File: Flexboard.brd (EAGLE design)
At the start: 488.2 x 145.3 mm, 452 parts, among them J1 USB4105-GF-A, SW1 1825910-7, U1 MK22FX512AVLQ12, U2 NCP1117ST33T3G, Y1 ABM3B-8.000MHZ-B2-T, Y2 ABS07-32.768KHZ-T

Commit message: added four media keys
added four additional media keys to board, and renumbered keys to
perserve correct numbering sequence.

Signed-off-by: Daniel DeGrasse <daniel@degrasse.com>
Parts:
- added D147, D148, D149: BAS16LT3G, BAS16LT3G:SOT95P240X111-3N
- added D150: UPS115UE3/TR7, UPS115UE3-TR7:UPS115UE3/TR7
- added KEY_146, KEY_147, KEY_148, KEY_149: CHERRY-MX-LED, cherrymx:CHERRY-MX-LED
- D146: value UPS115UE3/TR7 -> BAS16LT3G; device UPS115UE3-TR7:UPS115UE3/TR7 -> BAS16LT3G:SOT95P240X111-3N
- moved D41 411.1 mm to (428.6, 119.1)
- moved D42 411.1 mm to (447.7, 119.1)
- moved KEY_41 410.6 mm to (419.1, 114.3)
- moved KEY_42 410.6 mm to (438.1, 114.3)
- moved KEY_109 410.0 mm to (419.1, 47.6)
- moved KEY_64 410.0 mm to (419.1, 85.7)
- moved KEY_87 410.0 mm to (419.1, 66.7)
- moved D109 410.0 mm to (428.6, 45.2)
- moved D110 410.0 mm to (447.7, 45.2)
- moved D64 410.0 mm to (428.6, 83.3)
- moved D65 410.0 mm to (447.7, 83.3)
- moved D87 410.0 mm to (428.6, 64.3)
- moved D88 410.0 mm to (447.7, 64.3)
- moved KEY_110 410.0 mm to (438.1, 47.6)
- moved KEY_65 410.0 mm to (438.1, 85.7)
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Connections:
- new net N$155: D149.3, KEY_149.SW2
- new net N$159: D146.3, KEY_146.SW2
- new net N$161: D148.3, KEY_148.SW2
- new net N$165: D147.3, KEY_147.SW2
- net COL_10: now also KEY_100.SW1, KEY_122.SW1, KEY_54.SW1, KEY_77.SW1; no longer KEY_118.SW1, KEY_50.SW1, KEY_73.SW1, KEY_96.SW1
- net COL_11: now also KEY_101.SW1, KEY_123.SW1, KEY_55.SW1, KEY_78.SW1; no longer KEY_119.SW1, KEY_51.SW1, KEY_74.SW1, KEY_97.SW1
- net COL_12: now also KEY_102.SW1, KEY_124.SW1, KEY_139.SW1, KEY_56.SW1, KEY_79.SW1; no longer KEY_120.SW1, KEY_135.SW1, KEY_52.SW1, KEY_75.SW1, KEY_98.SW1
- net COL_13: now also KEY_103.SW1, KEY_125.SW1, KEY_140.SW1, KEY_57.SW1, KEY_80.SW1; no longer KEY_121.SW1, KEY_136.SW1, KEY_53.SW1, KEY_76.SW1, KEY_99.SW1
- net COL_14: now also KEY_104.SW1, KEY_141.SW1, KEY_58.SW1, KEY_81.SW1; no longer KEY_100.SW1, KEY_137.SW1, KEY_54.SW1, KEY_77.SW1
- net COL_15: now also KEY_59.SW1, KEY_82.SW1; no longer KEY_55.SW1, KEY_78.SW1
- net COL_17: now also KEY_105.SW1, KEY_126.SW1, KEY_142.SW1, KEY_60.SW1, KEY_83.SW1; no longer KEY_101.SW1, KEY_122.SW1, KEY_138.SW1, KEY_56.SW1, KEY_79.SW1
- net COL_18: now also KEY_106.SW1, KEY_127.SW1, KEY_143.SW1, KEY_61.SW1, KEY_84.SW1; no longer KEY_102.SW1, KEY_123.SW1, KEY_139.SW1, KEY_57.SW1, KEY_80.SW1
- net COL_19: now also KEY_107.SW1, KEY_128.SW1, KEY_144.SW1, KEY_62.SW1, KEY_85.SW1; no longer KEY_103.SW1, KEY_124.SW1, KEY_140.SW1, KEY_58.SW1, KEY_81.SW1
- net COL_1{SB}: now also KEY_113.SW1, KEY_133.SW1, KEY_45.SW1, KEY_68.SW1, KEY_91.SW1; no longer KEY_109.SW1, KEY_129.SW1, KEY_41.SW1, KEY_64.SW1, KEY_87.SW1
- net COL_20: now also KEY_108.SW1, KEY_129.SW1, KEY_145.SW1, KEY_63.SW1, KEY_86.SW1; no longer KEY_104.SW1, KEY_125.SW1, KEY_141.SW1, KEY_59.SW1, KEY_82.SW1
- net COL_21: now also KEY_109.SW1, KEY_130.SW1, KEY_146.SW1, KEY_41.SW1, KEY_64.SW1, KEY_87.SW1; no longer KEY_105.SW1, KEY_126.SW1, KEY_142.SW1, KEY_60.SW1, KEY_83.SW1
- net COL_22: now also KEY_110.SW1, KEY_131.SW1, KEY_147.SW1, KEY_42.SW1, KEY_65.SW1, KEY_88.SW1; no longer KEY_106.SW1, KEY_127.SW1, KEY_143.SW1, KEY_61.SW1, KEY_84.SW1
- net COL_23: now also KEY_111.SW1, KEY_132.SW1, KEY_148.SW1, KEY_43.SW1, KEY_66.SW1, KEY_89.SW1; no longer KEY_107.SW1, KEY_128.SW1, KEY_144.SW1, KEY_62.SW1, KEY_85.SW1
- net COL_24: now also KEY_112.SW1, KEY_149.SW1, KEY_44.SW1, KEY_67.SW1, KEY_90.SW1; no longer KEY_108.SW1, KEY_145.SW1, KEY_63.SW1, KEY_86.SW1
- net COL_2{SB}: now also KEY_114.SW1, KEY_134.SW1, KEY_46.SW1, KEY_69.SW1, KEY_92.SW1; no longer KEY_110.SW1, KEY_130.SW1, KEY_42.SW1, KEY_65.SW1, KEY_88.SW1
- net COL_3: now also KEY_115.SW1, KEY_135.SW1, KEY_47.SW1, KEY_70.SW1, KEY_93.SW1; no longer KEY_111.SW1, KEY_131.SW1, KEY_43.SW1, KEY_66.SW1, KEY_89.SW1
- net COL_4: now also KEY_116.SW1, KEY_136.SW1, KEY_48.SW1, KEY_71.SW1, KEY_94.SW1; no longer KEY_112.SW1, KEY_132.SW1, KEY_44.SW1, KEY_67.SW1, KEY_90.SW1
- net COL_5: now also KEY_117.SW1, KEY_137.SW1, KEY_49.SW1, KEY_72.SW1, KEY_95.SW1; no longer KEY_113.SW1, KEY_133.SW1, KEY_45.SW1, KEY_68.SW1, KEY_91.SW1
- net COL_6: now also KEY_118.SW1, KEY_50.SW1, KEY_73.SW1, KEY_96.SW1; no longer KEY_114.SW1, KEY_46.SW1, KEY_69.SW1, KEY_92.SW1
- net COL_7: now also KEY_119.SW1, KEY_51.SW1, KEY_74.SW1, KEY_97.SW1; no longer KEY_115.SW1, KEY_47.SW1, KEY_70.SW1, KEY_93.SW1
- net COL_8: now also KEY_120.SW1, KEY_138.SW1, KEY_52.SW1, KEY_75.SW1, KEY_98.SW1; no longer KEY_116.SW1, KEY_134.SW1, KEY_48.SW1, KEY_71.SW1, KEY_94.SW1
- net COL_9: now also KEY_121.SW1, KEY_53.SW1, KEY_76.SW1, KEY_99.SW1; no longer KEY_117.SW1, KEY_49.SW1, KEY_72.SW1, KEY_95.SW1
- net LED_COL_10: now also KEY_100.LED-, KEY_122.LED-, KEY_54.LED-, KEY_77.LED-; no longer KEY_118.LED-, KEY_50.LED-, KEY_73.LED-, KEY_96.LED-
- net LED_COL_11: now also KEY_101.LED-, KEY_123.LED-, KEY_55.LED-, KEY_78.LED-; no longer KEY_119.LED-, KEY_51.LED-, KEY_74.LED-, KEY_97.LED-
- net LED_COL_12: now also KEY_102.LED-, KEY_124.LED-, KEY_139.LED-, KEY_56.LED-, KEY_79.LED-; no longer KEY_120.LED-, KEY_135.LED-, KEY_52.LED-, KEY_75.LED-, KEY_98.LED-
- net LED_COL_13: now also KEY_103.LED-, KEY_125.LED-, KEY_140.LED-, KEY_57.LED-, KEY_80.LED-; no longer KEY_121.LED-, KEY_136.LED-, KEY_53.LED-, KEY_76.LED-, KEY_99.LED-
- net LED_COL_14: now also KEY_104.LED-, KEY_141.LED-, KEY_58.LED-, KEY_81.LED-; no longer KEY_100.LED-, KEY_137.LED-, KEY_54.LED-, KEY_77.LED-
- net LED_COL_15: now also KEY_59.LED-, KEY_82.LED-; no longer KEY_55.LED-, KEY_78.LED-
- net LED_COL_17: now also KEY_105.LED-, KEY_126.LED-, KEY_142.LED-, KEY_60.LED-, KEY_83.LED-; no longer KEY_101.LED-, KEY_122.LED-, KEY_138.LED-, KEY_56.LED-, KEY_79.LED-
- net LED_COL_18: now also KEY_106.LED-, KEY_127.LED-, KEY_143.LED-, KEY_61.LED-, KEY_84.LED-; no longer KEY_102.LED-, KEY_123.LED-, KEY_139.LED-, KEY_57.LED-, KEY_80.LED-
- net LED_COL_19: now also KEY_107.LED-, KEY_128.LED-, KEY_144.LED-, KEY_62.LED-, KEY_85.LED-; no longer KEY_103.LED-, KEY_124.LED-, KEY_140.LED-, KEY_58.LED-, KEY_81.LED-
- net LED_COL_1{SB}: now also KEY_113.LED-, KEY_133.LED-, KEY_45.LED-, KEY_68.LED-, KEY_91.LED-; no longer KEY_109.LED-, KEY_129.LED-, KEY_41.LED-, KEY_64.LED-, KEY_87.LED-
- net LED_COL_20: now also KEY_108.LED-, KEY_129.LED-, KEY_145.LED-, KEY_63.LED-, KEY_86.LED-; no longer KEY_104.LED-, KEY_125.LED-, KEY_141.LED-, KEY_59.LED-, KEY_82.LED-
- net LED_COL_21: now also KEY_109.LED-, KEY_130.LED-, KEY_146.LED-, KEY_41.LED-, KEY_64.LED-, KEY_87.LED-; no longer KEY_105.LED-, KEY_126.LED-, KEY_142.LED-, KEY_60.LED-, KEY_83.LED-
- net LED_COL_22: now also KEY_110.LED-, KEY_131.LED-, KEY_147.LED-, KEY_42.LED-, KEY_65.LED-, KEY_88.LED-; no longer KEY_106.LED-, KEY_127.LED-, KEY_143.LED-, KEY_61.LED-, KEY_84.LED-
- net LED_COL_23: now also KEY_111.LED-, KEY_132.LED-, KEY_148.LED-, KEY_43.LED-, KEY_66.LED-, KEY_89.LED-; no longer KEY_107.LED-, KEY_128.LED-, KEY_144.LED-, KEY_62.LED-, KEY_85.LED-
- net LED_COL_24: now also KEY_112.LED-, KEY_149.LED-, KEY_44.LED-, KEY_67.LED-, KEY_90.LED-; no longer KEY_108.LED-, KEY_145.LED-, KEY_63.LED-, KEY_86.LED-
- net LED_COL_2{SB}: now also KEY_114.LED-, KEY_134.LED-, KEY_46.LED-, KEY_69.LED-, KEY_92.LED-; no longer KEY_110.LED-, KEY_130.LED-, KEY_42.LED-, KEY_65.LED-, KEY_88.LED-
- net LED_COL_3: now also KEY_115.LED-, KEY_135.LED-, KEY_47.LED-, KEY_70.LED-, KEY_93.LED-; no longer KEY_111.LED-, KEY_131.LED-, KEY_43.LED-, KEY_66.LED-, KEY_89.LED-
- net LED_COL_4: now also KEY_116.LED-, KEY_136.LED-, KEY_48.LED-, KEY_71.LED-, KEY_94.LED-; no longer KEY_112.LED-, KEY_132.LED-, KEY_44.LED-, KEY_67.LED-, KEY_90.LED-
- net LED_COL_5: now also KEY_117.LED-, KEY_49.LED-, KEY_72.LED-, KEY_95.LED-; no longer KEY_113.LED-, KEY_45.LED-, KEY_68.LED-, KEY_91.LED-
- net LED_COL_6: now also KEY_118.LED-, KEY_50.LED-, KEY_73.LED-, KEY_96.LED-; no longer KEY_114.LED-, KEY_46.LED-, KEY_69.LED-, KEY_92.LED-
- net LED_COL_7: now also KEY_119.LED-, KEY_51.LED-, KEY_74.LED-, KEY_97.LED-; no longer KEY_115.LED-, KEY_47.LED-, KEY_70.LED-, KEY_93.LED-
- net LED_COL_8: now also KEY_120.LED-, KEY_138.LED-, KEY_52.LED-, KEY_75.LED-, KEY_98.LED-; no longer KEY_116.LED-, KEY_134.LED-, KEY_48.LED-, KEY_71.LED-, KEY_94.LED-
- net LED_COL_9: now also KEY_121.LED-, KEY_53.LED-, KEY_76.LED-, KEY_99.LED-; no longer KEY_117.LED-, KEY_49.LED-, KEY_72.LED-, KEY_95.LED-
- net LED_ROW_2{SB}: now also KEY_41.LED+, KEY_42.LED+, KEY_43.LED+, KEY_44.LED+
- net LED_ROW_3: now also KEY_45.LED+, KEY_46.LED+; no longer KEY_41.LED+, KEY_42.LED+
- net LED_ROW_3{SB}: now also KEY_60.LED+, KEY_61.LED+, KEY_62.LED+, KEY_63.LED+; no longer KEY_43.LED+, KEY_44.LED+, KEY_45.LED+, KEY_46.LED+
- net LED_ROW_4: now also KEY_68.LED+, KEY_69.LED+; no longer KEY_64.LED+, KEY_65.LED+
- net LED_ROW_4{SB}: now also KEY_83.LED+, KEY_84.LED+, KEY_85.LED+, KEY_86.LED+; no longer KEY_66.LED+, KEY_67.LED+, KEY_68.LED+, KEY_69.LED+
- net LED_ROW_5: now also KEY_91.LED+, KEY_92.LED+; no longer KEY_87.LED+, KEY_88.LED+
- net LED_ROW_5{SB}: now also KEY_105.LED+, KEY_106.LED+, KEY_107.LED+, KEY_108.LED+; no longer KEY_89.LED+, KEY_90.LED+, KEY_91.LED+, KEY_92.LED+
- net LED_ROW_6: now also KEY_113.LED+, KEY_114.LED+; no longer KEY_109.LED+, KEY_110.LED+
- net LED_ROW_6{SB}: now also KEY_126.LED+, KEY_127.LED+, KEY_128.LED+, KEY_129.LED+; no longer KEY_111.LED+, KEY_112.LED+, KEY_113.LED+, KEY_114.LED+
- net LED_ROW_7: now also KEY_133.LED+, KEY_134.LED+; no longer KEY_129.LED+, KEY_130.LED+
- net LED_ROW_7{SB}: now also KEY_142.LED+, KEY_143.LED+, KEY_144.LED+, KEY_145.LED+; no longer KEY_131.LED+, KEY_132.LED+, KEY_133.LED+, KEY_134.LED+
- net N$103: now also D109.1, D110.1, D111.1, D112.1; no longer D105.1, D106.1, D107.1, D108.1
- net N$124: now also D130.1, D131.1, D132.1; no longer D126.1, D127.1, D128.1
- net N$151: now also D146.1, D147.1, D148.1, D149.1; no longer D142.1, D143.1, D144.1, D145.1
- net N$170: now also KEY_64.LED+, KEY_65.LED+, KEY_66.LED+, KEY_67.LED+; no longer KEY_60.LED+, KEY_61.LED+, KEY_62.LED+, KEY_63.LED+
- net N$173: now also KEY_87.LED+, KEY_88.LED+, KEY_89.LED+, KEY_90.LED+; no longer KEY_83.LED+, KEY_84.LED+, KEY_85.LED+, KEY_86.LED+
- net N$179: now also KEY_109.LED+, KEY_110.LED+, KEY_111.LED+, KEY_112.LED+; no longer KEY_105.LED+, KEY_106.LED+, KEY_107.LED+, KEY_108.LED+
- net N$182: now also KEY_130.LED+, KEY_131.LED+, KEY_132.LED+; no longer KEY_126.LED+, KEY_127.LED+, KEY_128.LED+
- net N$185: now also KEY_146.LED+, KEY_147.LED+, KEY_148.LED+, KEY_149.LED+; no longer KEY_142.LED+, KEY_143.LED+, KEY_144.LED+, KEY_145.LED+
- net N$65: now also D64.1, D65.1, D66.1, D67.1; no longer D60.1, D61.1, D62.1, D63.1
- net N$79: now also D87.1, D88.1, D89.1, D90.1; no longer D83.1, D84.1, D85.1, D86.1
- net ROW_2{SB}: now also D41.1, D42.1, D43.1, D44.1
- net ROW_3: now also D45.1, D46.1; no longer D41.1, D42.1
- net ROW_3{SB}: now also D60.1, D61.1, D62.1, D63.1; no longer D43.1, D44.1, D45.1, D46.1
- net ROW_4: now also D68.1, D69.1; no longer D64.1, D65.1
- net ROW_4{SB}: now also D83.1, D84.1, D85.1, D86.1; no longer D66.1, D67.1, D68.1, D69.1
- net ROW_5: now also D91.1, D92.1; no longer D87.1, D88.1
- net ROW_5{SB}: now also D105.1, D106.1, D107.1, D108.1; no longer D89.1, D90.1, D91.1, D92.1
- net ROW_6: now also D113.1, D114.1; no longer D109.1, D110.1
- net ROW_6{SB}: now also D126.1, D127.1, D128.1, D129.1; no longer D111.1, D112.1, D113.1, D114.1
- net ROW_7: now also D133.1, D134.1; no longer D129.1, D130.1
- net ROW_7{SB}: now also D142.1, D143.1, D144.1, D145.1; no longer D131.1, D132.1, D133.1, D134.1
- net VLDO_5V5: now also D150.1; no longer D146.1
- net VSYS_5V5: now also D150.2; no longer D146.2
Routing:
- net ROW_2{SB}: track 375.2 -> 469.2 mm
- net LED_ROW_2{SB}: track 377.3 -> 466.8 mm
- net COL_24: track 99.6 -> 129.2 mm
- net COL_22: track 91.9 -> 121.3 mm
- net COL_21: track 88.7 -> 117.7 mm
- net COL_23: track 90.7 -> 115.4 mm, vias 0 -> 1
- net LED_COL_23: track 110.0 -> 131.3 mm
- net LED_COL_24: track 117.9 -> 139.0 mm
- net LED_COL_22: track 107.2 -> 127.5 mm
- net LED_COL_21: track 106.9 -> 127.1 mm
- net N$165: track 0.00 -> 11.2 mm
- net N$161: track 0.00 -> 11.2 mm
- net N$159: track 0.00 -> 11.2 mm
- net N$89: track 11.2 -> 0.00 mm
- net N$147: track 4.31 -> 11.2 mm
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
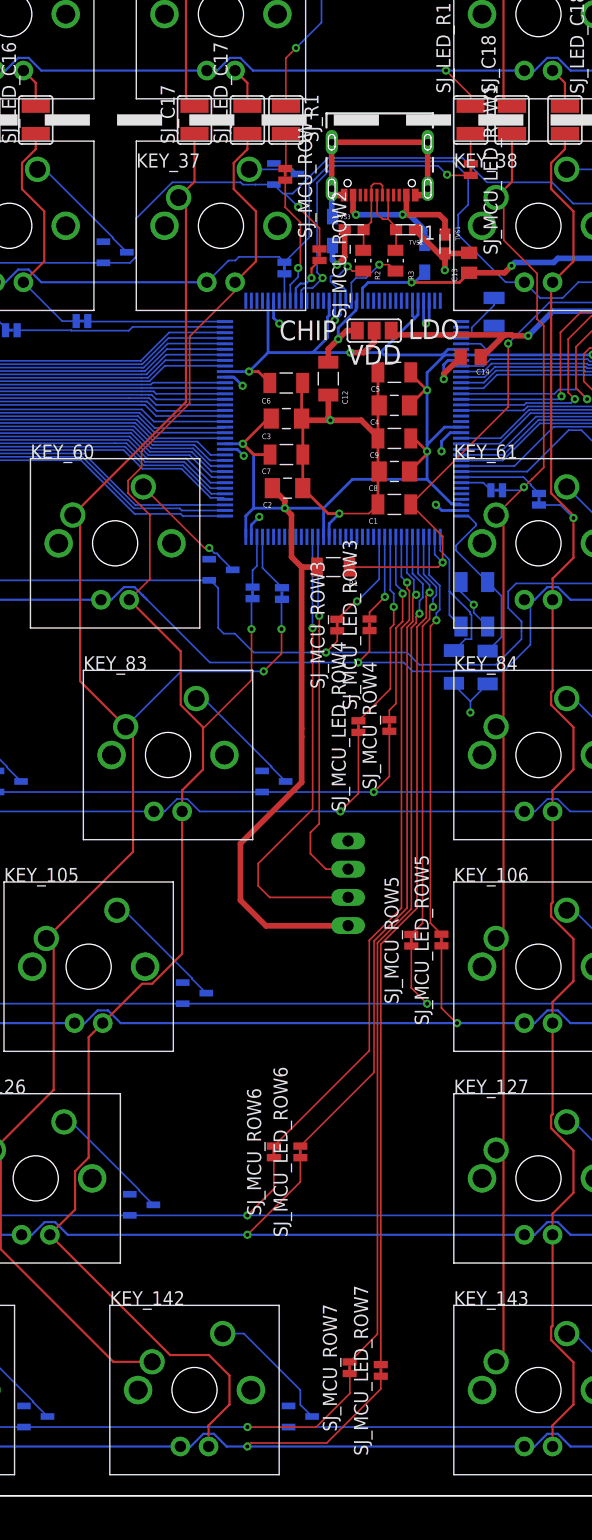
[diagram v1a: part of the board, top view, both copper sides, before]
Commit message: added current limiting resistors to LED rows
current limit resistors should limit LED network to 10mA across each
LED, for a total of roughly 70mA sourced from the chip.

Signed-off-by: Daniel DeGrasse <daniel@degrasse.com>
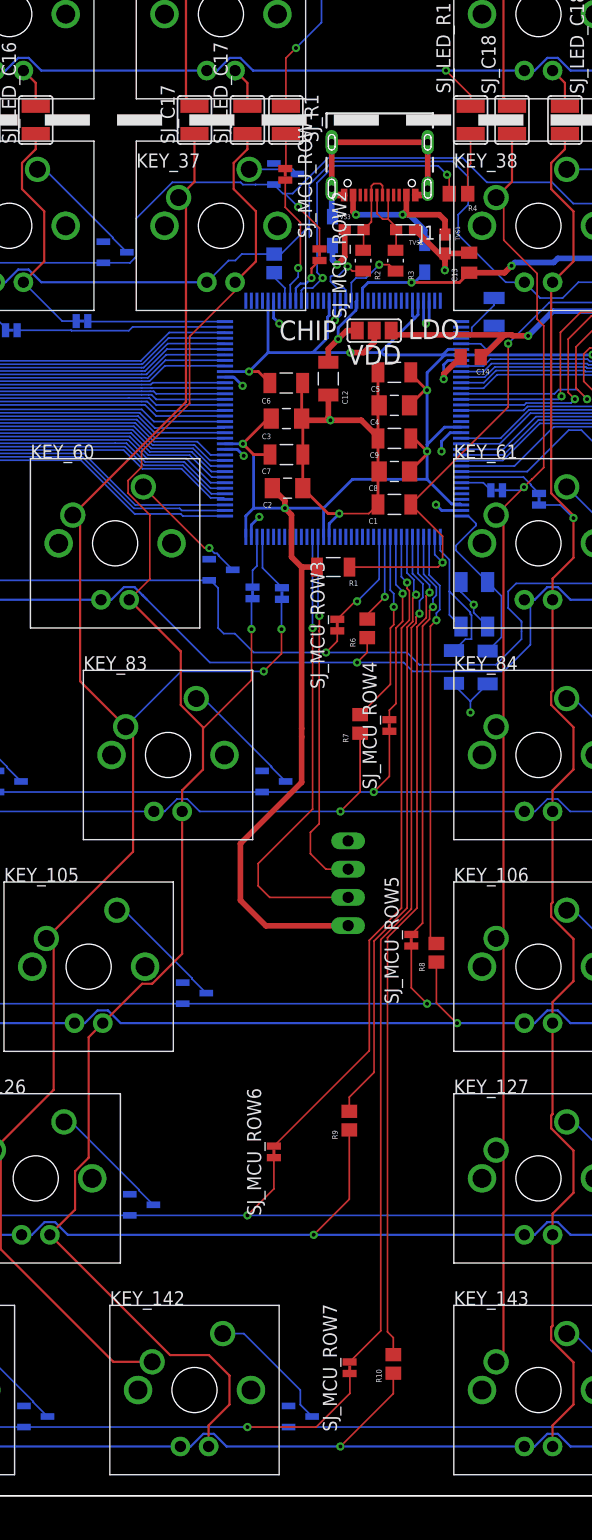
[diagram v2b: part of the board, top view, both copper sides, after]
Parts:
- removed SJ_MCU_LED_ROW1, SJ_MCU_LED_ROW2, SJ_MCU_LED_ROW3, SJ_MCU_LED_ROW4, SJ_MCU_LED_ROW5, SJ_MCU_LED_ROW6, SJ_MCU_LED_ROW7: JUMPER-SMT_2_NC_TRACE_NO-SILK, SparkFun-Jumpers:SMT-JUMPER_2_NC_TRACE_NO-SILK
- added R10, R4, R5, R6, R7, R8, R9: RNCP0805FTD20R0, RNCP0805FTD20R0:RESC2012X60N
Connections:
- net LED_ROW_1{MCU}: now also R4.2; no longer SJ_MCU_LED_ROW1.2
- net LED_ROW_1{SB}: now also R4.1; no longer SJ_MCU_LED_ROW1.1
- net LED_ROW_2{MCU}: now also R5.2; no longer SJ_MCU_LED_ROW2.2
- net LED_ROW_2{SB}: now also R5.1; no longer SJ_MCU_LED_ROW2.1
- net LED_ROW_3{MCU}: now also R6.2; no longer SJ_MCU_LED_ROW3.2
- net LED_ROW_3{SB}: now also R6.1; no longer SJ_MCU_LED_ROW3.1
- net LED_ROW_4{MCU}: now also R7.2; no longer SJ_MCU_LED_ROW4.2
- net LED_ROW_4{SB}: now also R7.1; no longer SJ_MCU_LED_ROW4.1
- net LED_ROW_5{MCU}: now also R8.2; no longer SJ_MCU_LED_ROW5.2
- net LED_ROW_5{SB}: now also R8.1; no longer SJ_MCU_LED_ROW5.1
- net LED_ROW_6{MCU}: now also R9.2; no longer SJ_MCU_LED_ROW6.2
- net LED_ROW_6{SB}: now also R9.1; no longer SJ_MCU_LED_ROW6.1
- net LED_ROW_7{MCU}: now also R10.2; no longer SJ_MCU_LED_ROW7.2
- net LED_ROW_7{SB}: now also R10.1; no longer SJ_MCU_LED_ROW7.1
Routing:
- net LED_ROW_7{SB}: track 380.5 -> 373.8 mm
- net LED_ROW_6{MCU}: track 59.5 -> 54.5 mm
- net LED_ROW_1{SB}: track 2.68 -> 5.47 mm
- net LED_ROW_6{SB}: track 379.6 -> 381.5 mm
- net LED_ROW_5{SB}: track 380.3 -> 379.0 mm
- net LED_ROW_7{MCU}: track 76.7 -> 75.8 mm
- net LED_ROW_5{MCU}: track 36.9 -> 37.6 mm
- net LED_ROW_4{MCU}: track 18.0 -> 17.4 mm
- net LED_ROW_3{SB}: track 385.3 -> 384.8 mm

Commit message: cleaned up name locations on board
cleaned up name locations on board silkscreen to ensure that there will
not be overlap between board printing and solder pads

Signed-off-by: Daniel DeGrasse <daniel@degrasse.com>
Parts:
- renumbered U$1 to J2
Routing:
- net N$89: track 0.00 -> 4.44 mm
- net ROW_4{SB}: track 381.1 -> 376.7 mm
- net LED_ROW_2{SB}: track 466.8 -> 465.8 mm
- net COL_2{SB}: track 150.3 -> 149.7 mm
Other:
- board text added: "U1"
- board text removed: "Cut Point"

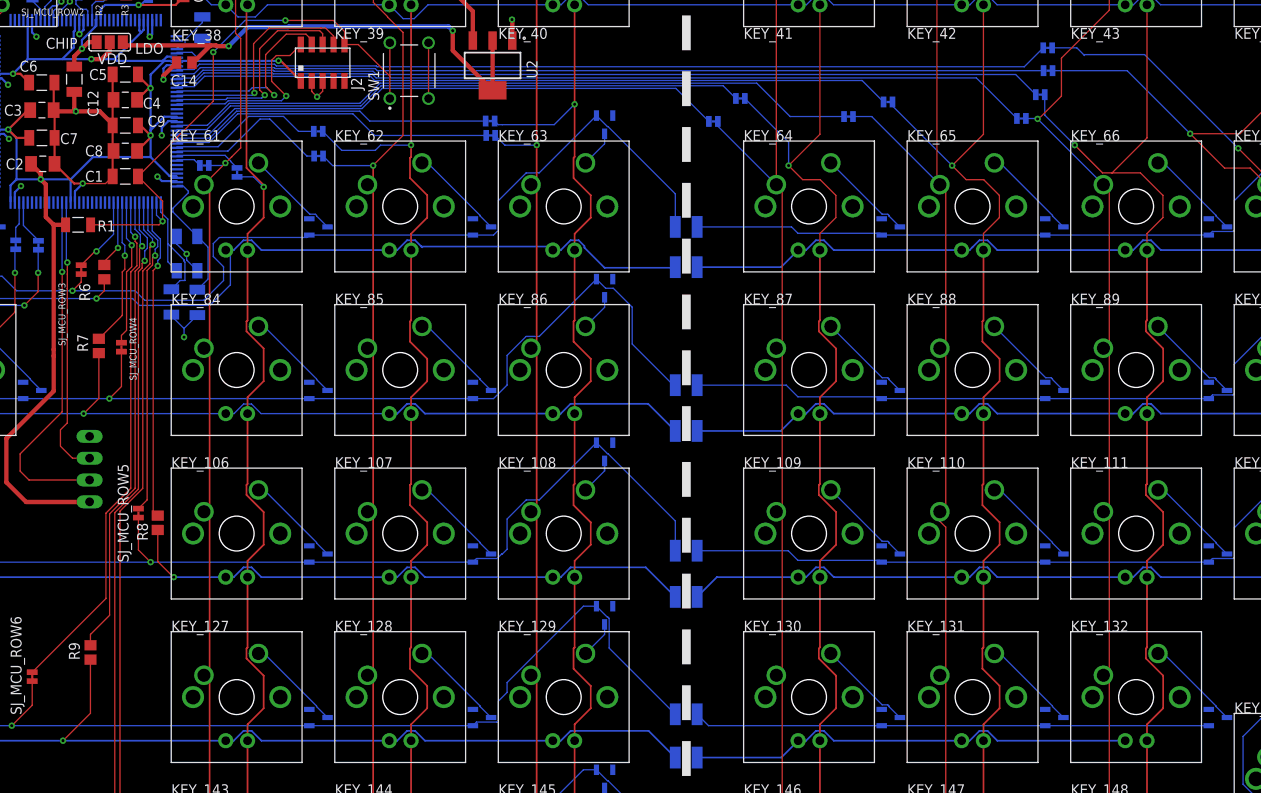
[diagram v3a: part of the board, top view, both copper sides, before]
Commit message: Fixed ERC errors
Fixed valid ERC errors, and approved remaining overlap warnings as
nonissues

Signed-off-by: Daniel DeGrasse <daniel@degrasse.com>
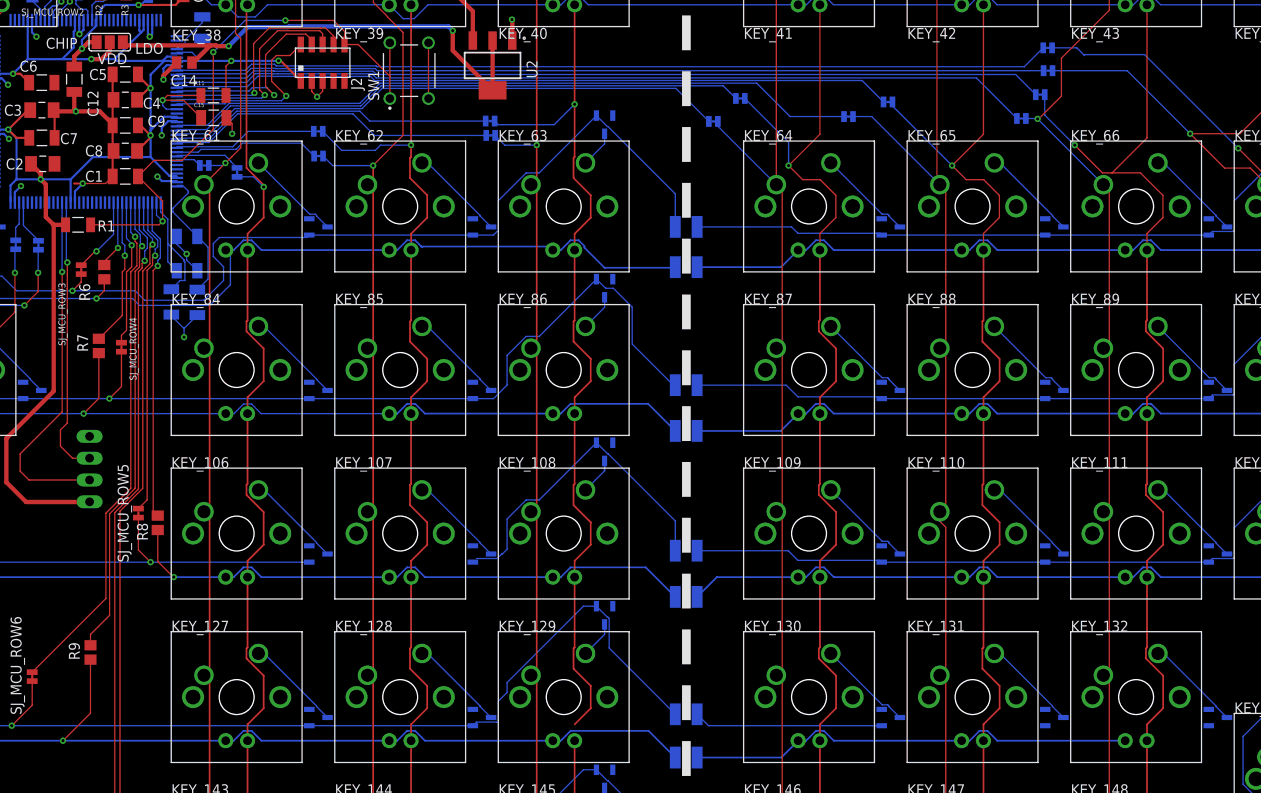
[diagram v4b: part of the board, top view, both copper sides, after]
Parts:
- added C15: 1000pF, C1206C102K1RACAUTO:CAPC3216X110N
- added R11: 10k, CRGCQ1206J10K:RESC3115X65N
- renumbered SJ__LED_R4_0 to SJ_LED_R4_0
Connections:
- net GND: now also C15.2
- net NMI: now also C15.1, R11.1
- net VDD_3V3: now also R11.2
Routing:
- net N$2: track 60.2 -> 22.1 mm
- net ROW_5{SB}: track 376.1 -> 356.4 mm
- net NMI: track 0.00 -> 12.5 mm, vias 0 -> 1
- net GND: track 106.9 -> 99.5 mm, vias 17 -> 18
- net VDD_3V3: track 180.7 -> 184.9 mm, vias 7 -> 8
- net COL_19{MCU}: track 19.3 -> 17.0 mm
- net RESET: track 67.9 -> 69.8 mm
- net LED_COL_20: track 139.0 -> 137.1 mm
- net LED_COL_19{MCU}: track 18.1 -> 16.7 mm

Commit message: ran DRC, fixed majority of errors
Fixed majority of DRC errors for JLPCB design rules. Still need to
check dimension and overlap errors on solder bridges.

Signed-off-by: Daniel DeGrasse <daniel@degrasse.com>
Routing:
- net N$2: track 22.1 -> 60.2 mm
- net ROW_5{SB}: track 356.4 -> 377.1 mm
- net LED_COL_20: track 137.1 -> 143.0 mm
- net LED_COL_2{SB}: track 150.2 -> 156.0 mm
- net JTAG_TMS/SWD_DIO: track 22.1 -> 26.5 mm
- net LED_COL_19: track 140.0 -> 144.2 mm
- net LED_COL_18: track 132.1 -> 136.1 mm
- net LED_COL_21: track 127.1 -> 131.0 mm
- net N$73: track 11.2 -> 15.0 mm
- net LED_COL_1{SB}: track 173.0 -> 176.8 mm
- net LED_ROW_1: track 403.1 -> 406.8 mm
- net ROW_2{SB}: track 469.2 -> 472.9 mm
- net LED_ROW_2{SB}: track 465.8 -> 469.3 mm
- net N$102: track 11.2 -> 14.7 mm
- net N$78: track 11.2 -> 14.6 mm
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
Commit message: added board dimensions and approved remaining DRC issues
added required board dimensions, and verified remaining DRC issues will
not cause problems

Signed-off-by: Daniel DeGrasse <daniel@degrasse.com>
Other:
- board size 488.2 x 145.3 mm -> 488.2 x 142.9 mm

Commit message: added mounting standoffs
mounting standoffs added for stability

Signed-off-by: Daniel DeGrasse <daniel@degrasse.com>
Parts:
- moved SJ_LED_R3_1 3.80 mm to (408.6, 78.6)
- moved SJ_R3_1 3.80 mm to (408.6, 83.3)
- moved SJ_R4_1 3.72 mm to (408.5, 64.5)
- moved SJ_R7_1 3.71 mm to (408.5, 9.32)
- moved SJ_R6_1 3.71 mm to (408.5, 26.4)
- moved SJ_LED_R4_1 3.70 mm to (408.5, 59.5)
- moved SJ_LED_R5_1 3.70 mm to (408.5, 40.1)
- moved SJ_LED_R7_1 3.70 mm to (408.5, 4.66)
- moved SJ_R5_1 3.70 mm to (408.5, 45.5)
- moved SJ_LED_R6_1 3.62 mm to (408.4, 21.9)
- moved SJ_MCU_ROW6 2.55 mm to (326.1, 31.5)
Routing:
- net LED_ROW_5{SB}: track 381.8 -> 393.0 mm
- net LED_COL_1{SB}: track 176.8 -> 171.5 mm
- net ROW_7{SB}: track 385.9 -> 391.0 mm
- net COL_24{MCU}: track 101.2 -> 106.0 mm
- net LED_COL_24{MCU}: track 102.0 -> 106.8 mm
- net LED_COL_23{MCU}: track 101.3 -> 106.0 mm
- net COL_23{MCU}: track 100.1 -> 104.7 mm
- net LED_COL_22{MCU}: track 83.7 -> 88.1 mm
- net COL_2{MCU}: track 264.9 -> 269.2 mm
- net COL_1{SB}: track 172.5 -> 176.7 mm
- net ROW_4{SB}: track 377.4 -> 381.3 mm
- net N$79: track 81.4 -> 77.5 mm
- net N$65: track 81.1 -> 77.3 mm
- net N$2: track 60.2 -> 56.4 mm
- net N$151: track 92.6 -> 88.8 mm
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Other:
- board size 488.2 x 142.9 mm -> 492.9 x 143.1 mm

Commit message: Add files via upload
Added standoff locations (blind and thru)
Added stab mounts for Lshift, Rshift, Enter, must use plate mount stabs for backspace and numenter due to conflict with MCU and bottom right standoff, respectively
Rearranged some wires to make room for holes
Resized PCB to max dimensions based off case
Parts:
- added D151, D152, D153: BAS16LT3G, BAS16LT3G:SOT95P240X111-3N
- added D200: UPS115UE3/TR7, UPS115UE3-TR7:UPS115UE3/TR7
- added KEY_150, KEY_151, KEY_152, KEY_153: CHERRY-MX-LED, cherrymx:CHERRY-MX-LED
- added SJ_C21, SJ_C22, SJ_C23, SJ_C24, SJ_LED_C21, SJ_LED_C22, SJ_LED_C23, SJ_LED_C24: (no value), jumper:SJW
- D150: value UPS115UE3/TR7 -> BAS16LT3G; device UPS115UE3-TR7:UPS115UE3/TR7 -> BAS16LT3G:SOT95P240X111-3N
- moved D150 71.0 mm to (426.5, 138.1)
- moved D148 3.77 mm to (463.2, 5.74)
- moved SJ_MCU_ROW7 1.58 mm to (336.9, 11.0)
- moved D126 0.98 mm to (317.1, 27.1)
- moved D104 0.81 mm to (290.6, 46.0)
- moved D137 0.71 mm to (116.8, 7.84)
- moved D138 0.71 mm to (188.0, 7.84)
- moved D125 0.50 mm to (281.0, 26.7)
- moved D115 0.40 mm to (78.6, 26.6)
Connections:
- new net N$124: D152.3, KEY_152.SW2
- new net N$138: D153.3, KEY_153.SW2
- new net N$91: D150.3, KEY_150.SW2
- new net N$99: D151.3, KEY_151.SW2
- net COL_21: now also KEY_150.SW1, SJ_C21.1, SJ_C21.2
- net COL_22: now also KEY_151.SW1, SJ_C22.1, SJ_C22.2
- net COL_23: now also KEY_152.SW1, SJ_C23.1, SJ_C23.2
- net COL_24: now also KEY_153.SW1, SJ_C24.1, SJ_C24.2
- net LED_COL_21: now also KEY_150.LED-, SJ_LED_C21.1, SJ_LED_C21.2
- net LED_COL_22: now also KEY_151.LED-, SJ_LED_C22.1, SJ_LED_C22.2
- net LED_COL_23: now also KEY_152.LED-, SJ_LED_C23.1, SJ_LED_C23.2
- net LED_COL_24: now also KEY_153.LED-, SJ_LED_C24.1, SJ_LED_C24.2
- net LED_ROW_1: now also KEY_150.LED+, KEY_151.LED+, KEY_152.LED+, KEY_153.LED+
- net ROW_1: now also D150.1, D151.1, D152.1, D153.1
- net VLDO_5V5: now also D200.1; no longer D150.1
- net VSYS_5V5: now also D200.2; no longer D150.2
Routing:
- net LED_ROW_1: track 406.8 -> 496.6 mm
- net ROW_1: track 419.7 -> 509.3 mm
- net LED_COL_21: track 131.0 -> 150.0 mm
- net LED_COL_22: track 130.9 -> 149.8 mm
- net LED_COL_23: track 133.2 -> 152.1 mm
- net LED_COL_24: track 141.3 -> 160.2 mm
- net COL_22: track 121.3 -> 138.8 mm
- net COL_23: track 115.4 -> 132.9 mm
- net COL_24: track 129.2 -> 146.6 mm
- net COL_21: track 117.7 -> 134.9 mm
- net N$91: track 0.00 -> 3.93 mm
- net N$99: track 0.00 -> 3.38 mm
- net N$124: track 0.00 -> 3.33 mm
- net N$151: track 88.8 -> 91.9 mm
- net N$138: track 0.00 -> 2.78 mm
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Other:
- board size 492.9 x 143.1 mm -> 485.5 x 142.5 mm
